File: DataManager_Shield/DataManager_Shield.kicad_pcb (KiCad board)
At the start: 4 copper layers, 78 x 70 mm, 79 parts, among them J1 CAR_IN, J2 aux_pin, J3 CAR_OUT, J4 Mode_Selector, K1 IM03, K2 IM03, Q10 AO3400A, Q9 AO3400A, U1 TLP291-4, U2 MCP4725xxx-xCH, U3 TLP291-4, U4 PCA9306

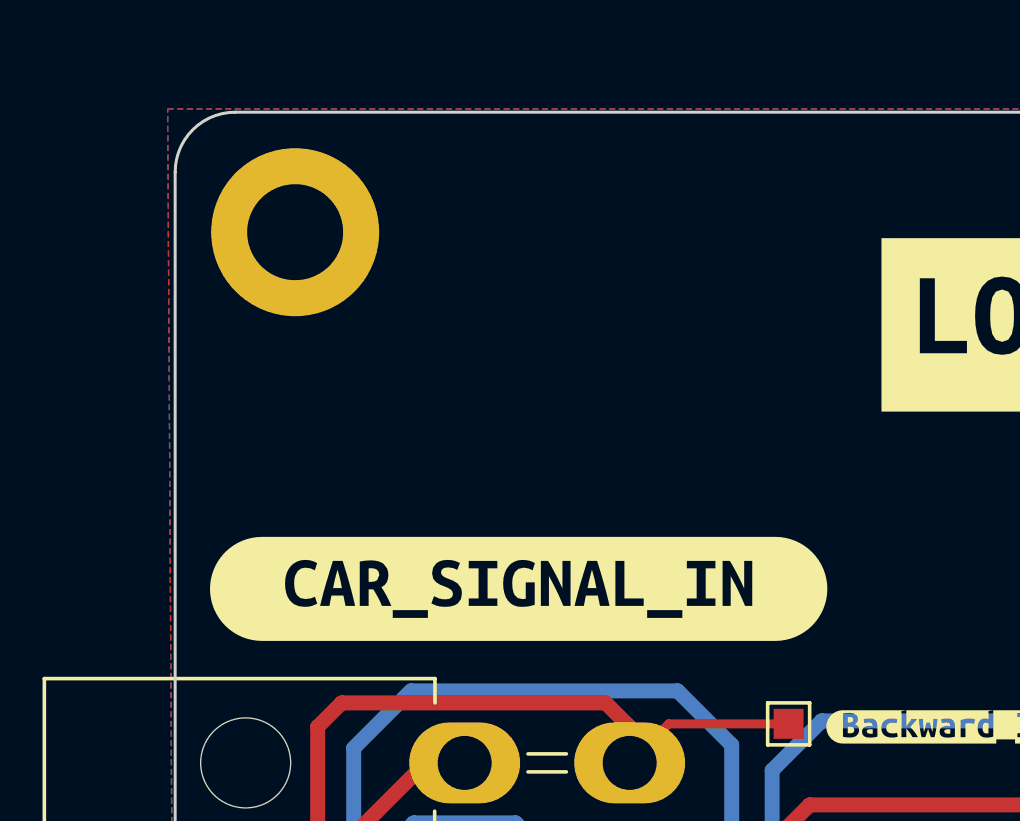
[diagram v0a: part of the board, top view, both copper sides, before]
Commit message: Fix PCB Isolate GND
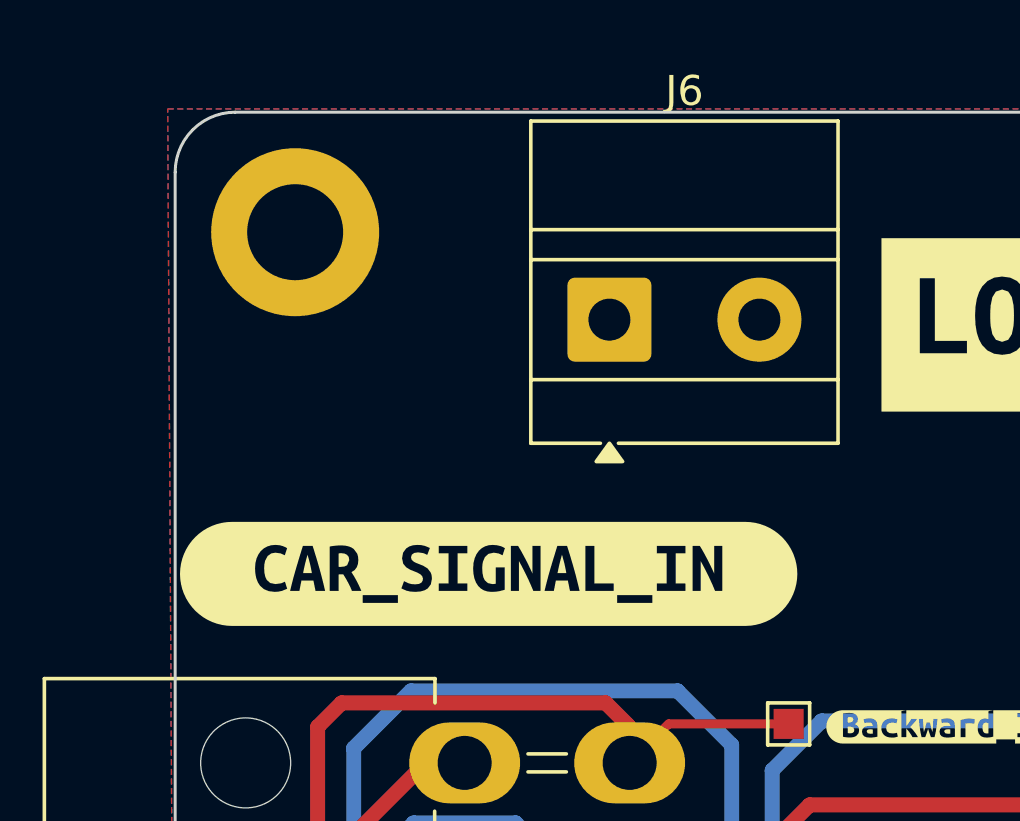
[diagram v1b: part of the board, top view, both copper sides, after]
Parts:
- added J6: Screw_Terminal_01x02, TerminalBlock_MetzConnect:TerminalBlock_MetzConnect_Type011_RT05502HBLC_1x02_P5.00mm_Horizontal, F.Cu at (93.5, 43.0)
- R26: value 15k -> 1.5M
- R5: value 10k -> 1M
- moved kibuzzard-6A36AE6B 1.12 mm to (89.5, 51.5)
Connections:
- J1 pad 3: /Relays/Pot_Low_out -> GND
- J3 pad 3: /Relays/Pot_Low_out -> GND
- R19 pad 2: GND -> B-
- R20 pad 2: GND -> B-
- R22 pad 2: GND -> B-
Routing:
- net /Relays/Pot_Low_out: track 97.9 -> 0.00 mm
- net GND: track 46.1 -> 138.6 mm, vias 21 -> 18
- net B-: track 0.00 -> 55.9 mm, vias 0 -> 3

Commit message: Update
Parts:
- J6: value Screw_Terminal_01x02 -> B-
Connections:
- U1 pad 4: GND -> B-
- U1 pad 6: GND -> B-
- U1 pad 8: GND -> B-
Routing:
- net B-: track 55.9 -> 88.0 mm, vias 3 -> 6
- net GND: track 138.6 -> 132.9 mm, vias 18 -> 15

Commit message: Seperate out GND_SPEED
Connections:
- D10 pad 1: GND -> GND_SPEED
- J1 pad 13: /Relays/Speed_Sensor_Return -> GND_SPEED
- J3 pad 13: /Relays/Speed_Sensor_Return -> GND_SPEED
- U1 pad 2: GND -> GND_SPEED
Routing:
- net GND_SPEED: track 0.00 -> 69.7 mm, vias 0 -> 3
- net /Relays/Speed_Sensor_Return: track 53.2 -> 0.00 mm
- net GND: track 132.9 -> 129.4 mm, vias 15 -> 13
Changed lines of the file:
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@@
 			(layers "*.Cu" "*.Mask")
 			(remove_unused_layers no)
-			(net "/Relays/Speed_Sensor_Return")
+			(net "GND_SPEED")
 			(pinfunction "Pin_13_13")
 			(pintype "passive")
@@
 			(layers "*.Cu" "*.Mask")
 			(remove_unused_layers no)
-			(net "/Relays/Speed_Sensor_Return")
+			(net "GND_SPEED")
 			(pinfunction "Pin_13_13")
 			(pintype "passive")
@@
 			(layers "F.Cu" "F.Mask" "F.Paste")
 			(roundrect_rratio 0.25)
-			(net "GND")
+			(net "GND_SPEED")
 			(pintype "passive")
 		)
@@
 			(layers "F.Cu" "F.Mask" "F.Paste")
 			(roundrect_rratio 0.25)
-			(net "GND")
+			(net "GND_SPEED")
 			(pinfunction "K_1")
 			(pintype "passive")
@@
 	)
 	(segment
-		(start 110.5 87.625)
-		(end 112.3625 87.625)
-		(width 0.5)
-		(layer "F.Cu")
-		(net "GND")
-	)
-	(segment
 		(start 106.9125 64.425)
 		(end 108.775 64.425)
@@
 	)
 	(segment
-		(start 108.1875 84.4)
-		(end 109.8 84.4)
-		(width 0.5)
-		(layer "F.Cu")
-		(net "GND")
-	)
-	(segment
 		(start 141.025 96.6)
 		(end 141.2625 96.6)
@@
 	)
 	(segment
-		(start 112.3625 87.625)
-		(end 112.3875 87.6)
-		(width 0.5)
-		(layer "F.Cu")
-		(net "GND")
-	)
-	(segment
 		(start 129 96.8)
 		(end 128.8 96.6)
@@
 	)
 	(via
-		(at 109.8 84.4)
-		(size 1)
-		(drill 0.5)
-		(layers "F.Cu" "B.Cu")
-		(net "GND")
-	)
-	(via
 		(at 128 82)
 		(size 1)
@@
 	)
 	(via
-		(at 112.3875 87.6)
-		(size 1)
-		(drill 0.5)
-		(layers "F.Cu" "B.Cu")
-		(net "GND")
-	)
-	(via
 		(at 128.8 96.6)
 		(size 0.6)
@@
 	)
 	(segment
-		(start 141.905 76.165)
-		(end 140.035 76.165)
-		(width 0.5)
-		(layer "B.Cu")
-		(net "/Relays/Speed_Sensor_Return")
-	)
-	(segment
-		(start 96.6 74.6)
-		(end 96.6 73.6)
-		(width 0.5)
-		(layer "B.Cu")
-		(net "/Relays/Speed_Sensor_Return")
-	)
-	(segment
-		(start 94.155 71.385)
-		(end 94.385 71.385)
-		(width 0.5)
-		(layer "B.Cu")
-		(net "/Relays/Speed_Sensor_Return")
-	)
-	(segment
-		(start 94.2 71.2)
-		(end 94.2 70.4)
-		(width 0.5)
-		(layer "B.Cu")
-		(net "/Relays/Speed_Sensor_Return")
-	)
-	(segment
-		(start 116.3 78.4)
-		(end 100.4 78.4)
-		(width 0.5)
-		(layer "B.Cu")
-		(net "/Relays/Speed_Sensor_Return")
-	)
-	(segment
-		(start 100.4 78.4)
-		(end 96.6 74.6)
-		(width 0.5)
-		(layer "B.Cu")
-		(net "/Relays/Speed_Sensor_Return")
-	)
-	(segment
-		(start 140 76.2)
-		(end 139.113503 76.2)
-		(width 0.5)
-		(layer "B.Cu")
-		(net "/Relays/Speed_Sensor_Return")
-	)
-	(segment
-		(start 96.6 73.6)
-		(end 94.2 71.2)
-		(width 0.5)
-		(layer "B.Cu")
-		(net "/Relays/Speed_Sensor_Return")
-	)
-	(segment
-		(start 140.035 76.165)
-		(end 140 76.2)
-		(width 0.5)
-		(layer "B.Cu")
-		(net "/Relays/Speed_Sensor_Return")
-	)
-	(segment
-		(start 139.013503 76.3)
-		(end 118.4 76.3)
-		(width 0.5)
-		(layer "B.Cu")
-		(net "/Relays/Speed_Sensor_Return")
-	)
-	(segment
-		(start 139.113503 76.2)
-		(end 139.013503 76.3)
-		(width 0.5)
-		(layer "B.Cu")
-		(net "/Relays/Speed_Sensor_Return")
-	)
-	(segment
-		(start 118.4 76.3)
-		(end 116.3 78.4)
-		(width 0.5)
-		(layer "B.Cu")
-		(net "/Relays/Speed_Sensor_Return")
-	)
-	(segment
 		(start 101.525 86.4)
 		(end 101.525 84.8375)
@@
 		(net "Net-(D8-K)")
 	)
+	(segment
+		(start 110.5 87.625)
+		(end 112.3625 87.625)
+		(width 0.5)
+		(layer "F.Cu")
+		(net "GND_SPEED")
+	)
+	(segment
+		(start 108.1875 84.4)
+		(end 109.8 84.4)
+		(width 0.5)
+		(layer "F.Cu")
+		(net "GND_SPEED")
+	)
+	(segment
+		(start 112.3625 87.625)
+		(end 112.3875 87.6)
+		(width 0.5)
+		(layer "F.Cu")
+		(net "GND_SPEED")
+	)
+	(via
+		(at 116 78.45)
+		(size 0.6)
+		(drill 0.3)
+		(layers "F.Cu" "B.Cu")
+		(net "GND_SPEED")
+	)
+	(via
+		(at 109.8 84.4)
+		(size 1)
+		(drill 0.5)
+		(layers "F.Cu" "B.Cu")
+		(net "GND_SPEED")
+	)
+	(via
+		(at 112.3875 87.6)
+		(size 1)
+		(drill 0.5)
+		(layers "F.Cu" "B.Cu")
+		(net "GND_SPEED")
+	)
+	(segment
+		(start 141.905 76.165)
+		(end 140.035 76.165)
+		(width 0.5)
+		(layer "B.Cu")
+		(net "GND_SPEED")
+	)
+	(segment
+		(start 96.6 74.6)
+		(end 96.6 73.6)
+		(width 0.5)
+		(layer "B.Cu")
+		(net "GND_SPEED")
+	)
+	(segment
+		(start 94.155 71.385)
+		(end 94.385 71.385)
+		(width 0.5)
+		(layer "B.Cu")
+		(net "GND_SPEED")
+	)
+	(segment
+		(start 94.2 71.2)
+		(end 94.2 70.4)
+		(width 0.5)
+		(layer "B.Cu")
+		(net "GND_SPEED")
+	)
+	(segment
+		(start 116.3 78.4)
+		(end 100.4 78.4)
+		(width 0.5)
+		(layer "B.Cu")
+		(net "GND_SPEED")
+	)
+	(segment
+		(start 100.4 78.4)
+		(end 96.6 74.6)
+		(width 0.5)
+		(layer "B.Cu")
+		(net "GND_SPEED")
+	)
+	(segment
+		(start 140 76.2)
+		(end 139.113503 76.2)
+		(width 0.5)
+		(layer "B.Cu")
+		(net "GND_SPEED")
+	)
+	(segment
+		(start 96.6 73.6)
+		(end 94.2 71.2)
+		(width 0.5)
+		(layer "B.Cu")
+		(net "GND_SPEED")
+	)
+	(segment
+		(start 140.035 76.165)
+		(end 140 76.2)
+		(width 0.5)
+		(layer "B.Cu")
+		(net "GND_SPEED")
+	)
+	(segment
+		(start 139.013503 76.3)
+		(end 118.4 76.3)
+		(width 0.5)
+		(layer "B.Cu")
+		(net "GND_SPEED")
+	)
+	(segment
+		(start 139.113503 76.2)
+		(end 139.013503 76.3)
+		(width 0.5)
+		(layer "B.Cu")
+		(net "GND_SPEED")
+	)
+	(segment
+		(start 118.4 76.3)
+		(end 116.3 78.4)
+		(width 0.5)
+		(layer "B.Cu")
+		(net "GND_SPEED")
+	)
+	(segment
+		(start 110.05 84.4)
+		(end 116 78.45)
+		(width 0.5)
+		(layer "In1.Cu")
+		(net "GND_SPEED")
+	)
+	(segment
+		(start 109.8 84.4)
+		(end 110.05 84.4)
+		(width 0.5)
+		(layer "In1.Cu")
+		(net "GND_SPEED")
+	)
+	(segment
+		(start 109.8 84.4)
+		(end 109.8 85.0125)
+		(width 0.5)
+		(layer "In1.Cu")
+		(net "GND_SPEED")
+	)
+	(segment
+		(start 109.8 85.0125)
+		(end 112.3875 87.6)
+		(width 0.5)
+		(layer "In1.Cu")
+		(net "GND_SPEED")
+	)
 	(zone

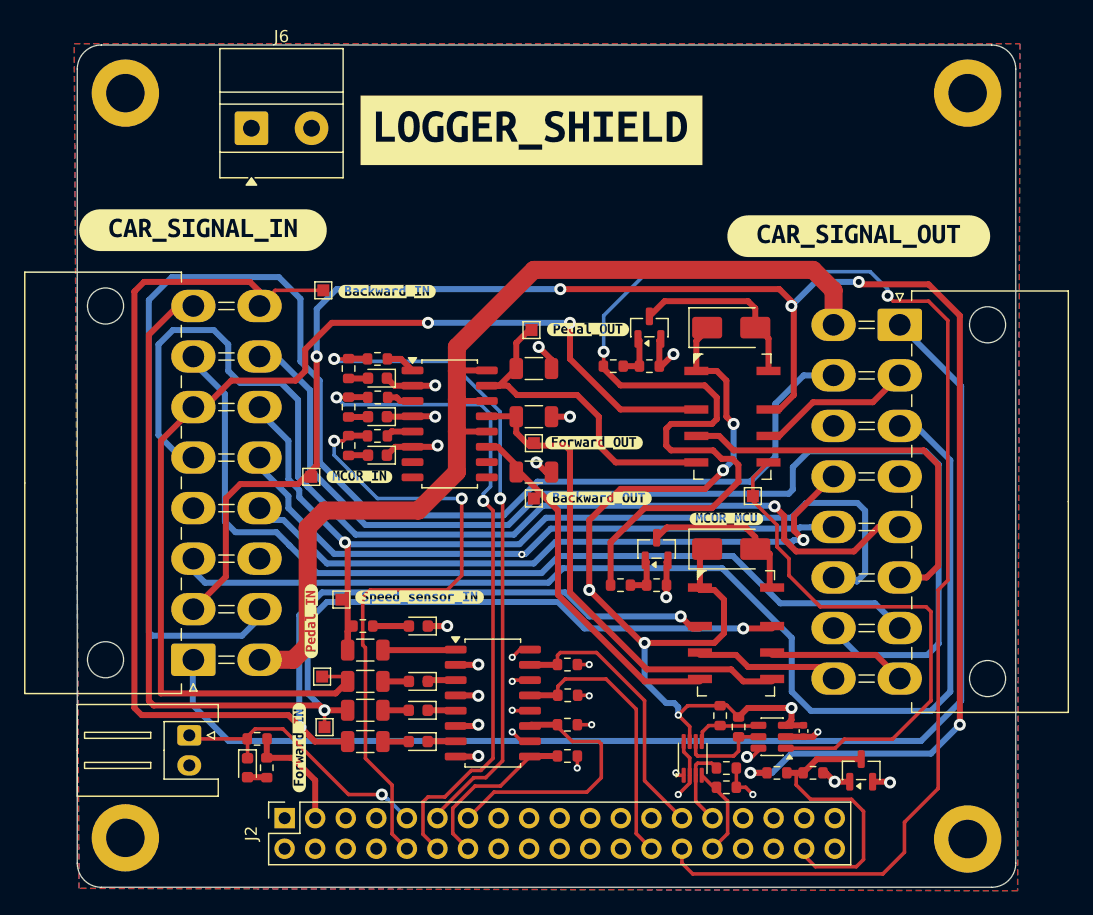
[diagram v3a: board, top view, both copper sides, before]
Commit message: Data logger board Major Fixes - Remove Speed Sensor's LED and increase R value - Remove Pedal level reader - Remove aux pin header from BoM, self soldering
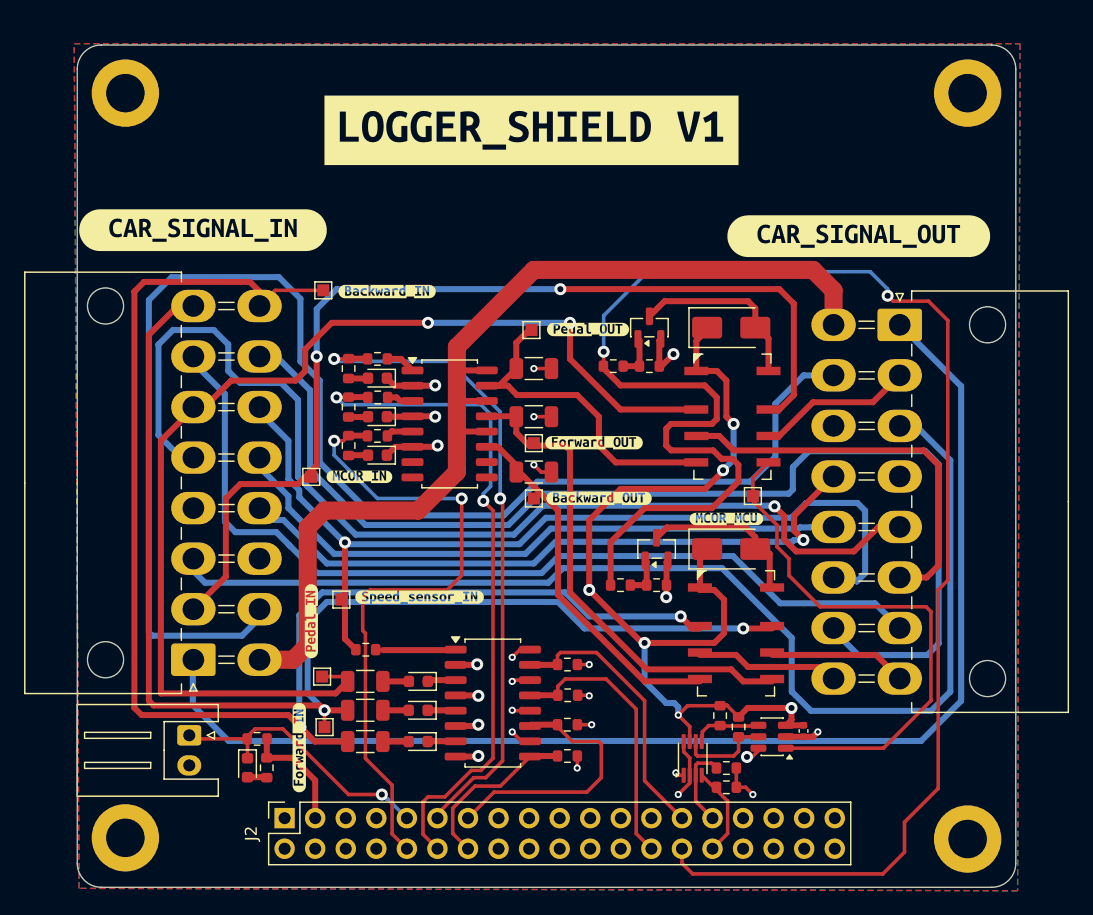
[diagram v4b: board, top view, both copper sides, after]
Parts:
- removed D10: LED, LED_SMD:LED_0603_1608Metric
- removed D3: BAT54S, Package_TO_SOT_SMD:SOT-23
- removed J6: B-, TerminalBlock_MetzConnect:TerminalBlock_MetzConnect_Type011_RT05502HBLC_1x02_P5.00mm_Horizontal
- removed R26: 1.5M, Resistor_SMD:R_0603_1608Metric
- removed R27: 1k, Resistor_SMD:R_0603_1608Metric
- removed R29: 470, Resistor_SMD:R_1206_3216Metric
- removed R5: 1M, Resistor_SMD:R_0603_1608Metric
- removed kibuzzard-6A36C52F: G***, kibuzzard-6A36C52F
- added R32: 4.7k, Resistor_SMD:R_0603_1608Metric, F.Cu at (103.0, 86.4)
- added kibuzzard-6AB2994C: G***, kibuzzard-6AB2994C, F.Cu at (116.8, 43.2)
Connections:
- J1 pad 13: GND_SPEED -> /Relays/Speed_Sensor_Return
- J3 pad 13: GND_SPEED -> /Relays/Speed_Sensor_Return
- R19 pad 2: B- -> GND
- R20 pad 2: B- -> GND
- R22 pad 2: B- -> GND
- U1 pad 2: GND_SPEED -> GND
- U1 pad 4: B- -> GND
- U1 pad 6: B- -> GND
- U1 pad 8: B- -> GND
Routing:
- net B-: track 88.0 -> 0.00 mm, vias 6 -> 0
- net /Relays/MCOR_Speed_Control_IN: track 154.5 -> 84.0 mm, vias 6 -> 2
- net GND_SPEED: track 69.7 -> 0.00 mm, vias 3 -> 0
- net /Relays/Speed_Sensor_Return: track 0.00 -> 53.2 mm
- net /aux_pins/ADC1_IN2: track 24.4 -> 0.00 mm
- net +3V3: track 85.8 -> 72.4 mm, vias 7 -> 6
- net GND: track 129.4 -> 139.1 mm, vias 13 -> 19
- net Net-(D10-A): track 3.00 -> 0.00 mm
- net /Relays/Speed_Sensor: track 78.2 -> 76.4 mm

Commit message: Isolate B-
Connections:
- J1 pad 3: GND -> B-
- J3 pad 3: GND -> B-
- R19 pad 2: GND -> B-
- R20 pad 2: GND -> B-
- R22 pad 2: GND -> B-
- U1 pad 2: GND -> B-
- U1 pad 4: GND -> B-
- U1 pad 6: GND -> B-
- U1 pad 8: GND -> B-
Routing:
- net B-: track 0.00 -> 145.7 mm, vias 0 -> 8
- net GND: track 139.1 -> 29.0 mm, vias 19 -> 12
